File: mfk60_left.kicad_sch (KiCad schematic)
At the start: 27 parts, among them J1 USB_C_Receptacle_USB2.0, J2 ISP, J3 TRRS Jack, SW1 RST, T1 Tab, T2 Tab, T3 Tab, U1 ATmega32U4-M, Y1 16M

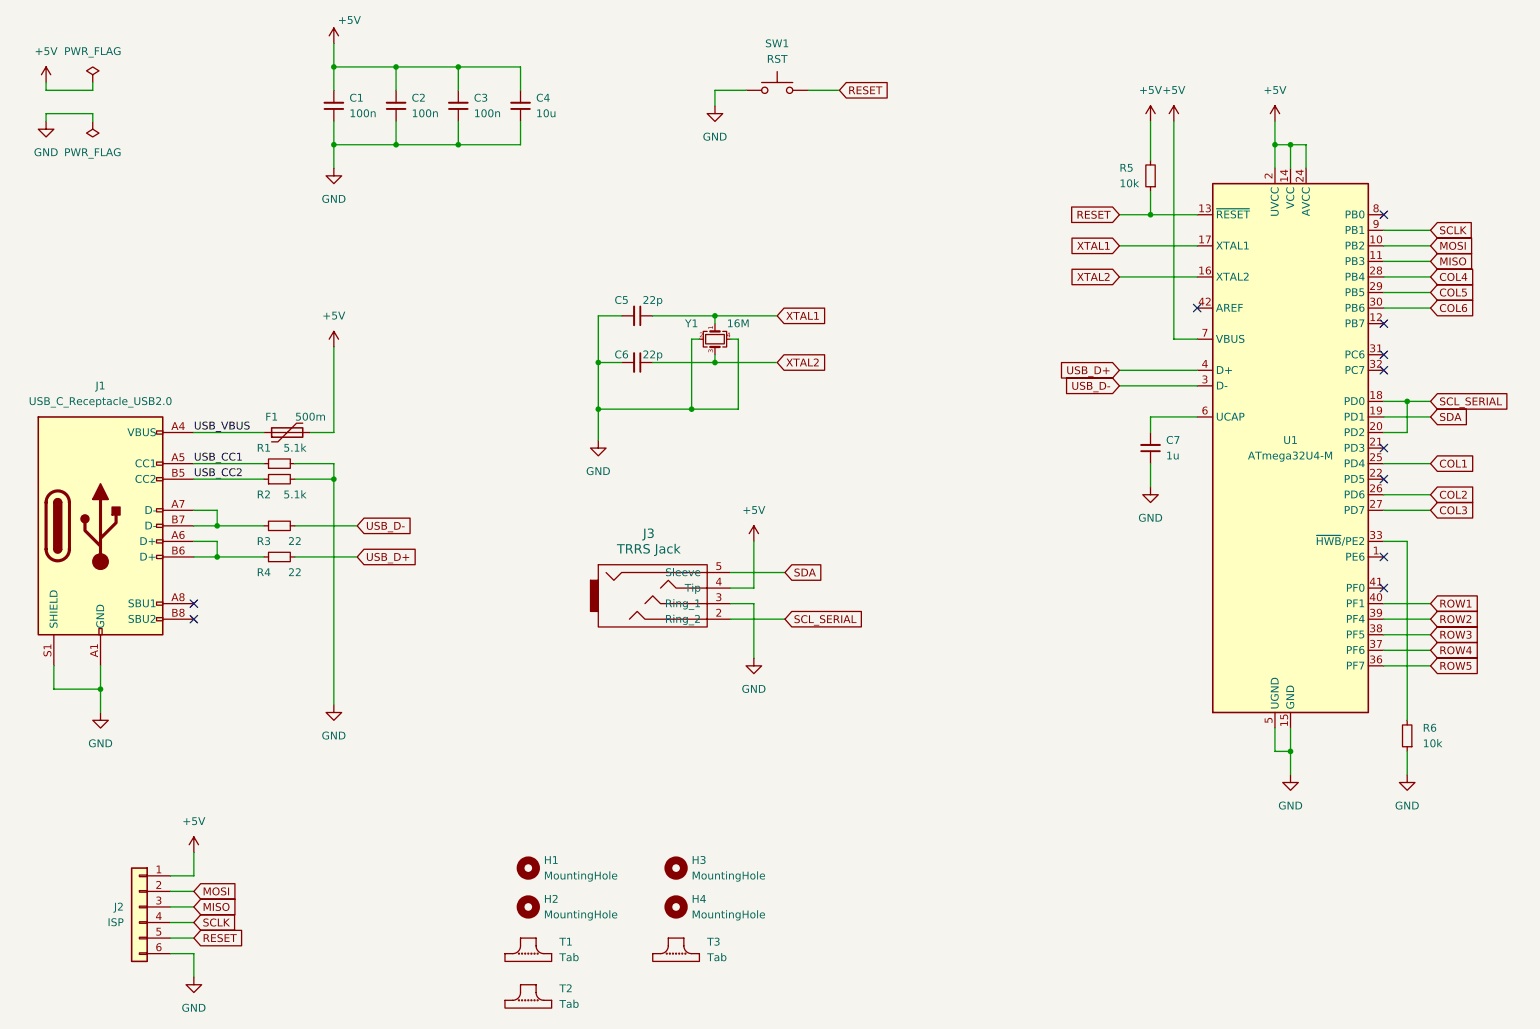
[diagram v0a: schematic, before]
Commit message: Add pull-up resistor on left side.
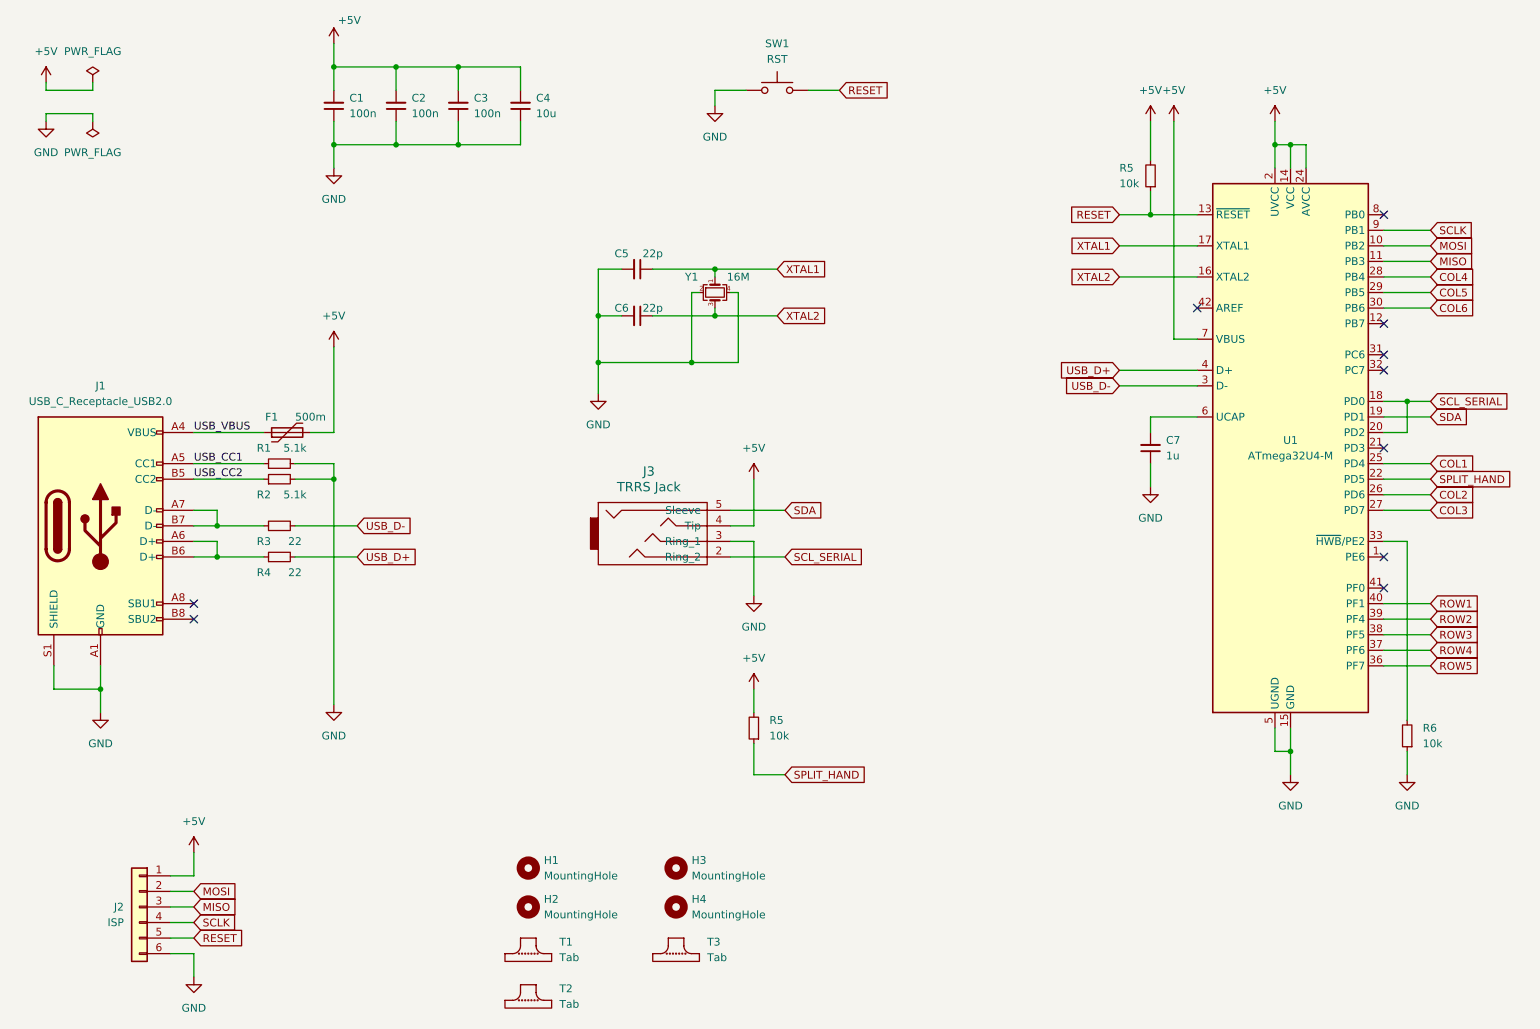
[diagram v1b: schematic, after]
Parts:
- added R5: 10k, Resistor_SMD:R_0805_2012Metric_Pad1.20x1.40mm_HandSolder, symbol Device:R_Small
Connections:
- net +5V: now also R5.2
- net SPLIT_HAND: now reaches U1.22 (PD5)
- net SPLIT_HAND: now also R5.1
- no-connect marks 11 -> 10
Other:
- moved on the sheet: C5, C6, J3, Y1

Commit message: FIX: key and diode value
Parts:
- J3: LCSC (none) -> C431535
- SW1: LCSC (none) -> C139797
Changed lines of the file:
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@@
+      (effects (font (size 1.27 1.27)) hide)
+    )
+    (property "Matrix" "" (at 226.06 91.44 0)
       (effects (font (size 1.27 1.27)) hide)
     )
@@
       (effects (font (size 1.27 1.27)) hide)
     )
+    (property "Matrix" "" (at 101.6 166.37 0)
+      (effects (font (size 1.27 1.27)) hide)
+    )
     (instances
       (project "mfk60"
@@
     )
     (property "LCSC" "C1804" (at 119.38 69.85 0)
+      (effects (font (size 1.27 1.27)) hide)
+    )
+    (property "Matrix" "" (at 119.38 69.85 0)
       (effects (font (size 1.27 1.27)) hide)
     )
@@
       (effects (font (size 1.27 1.27)) hide)
     )
+    (property "Matrix" "" (at 203.2 46.99 0)
+      (effects (font (size 1.27 1.27)) hide)
+    )
     (pin "1")
     (pin "2")
@@
     )
     (property "Datasheet" "~" (at 142.24 27.94 0)
+      (effects (font (size 1.27 1.27)) hide)
+    )
+    (property "Matrix" "" (at 142.24 33.02 0)
+      (effects (font (size 1.27 1.27)) hide)
+    )
+    (property "LCSC" "C139797" (at 142.24 33.02 0)
       (effects (font (size 1.27 1.27)) hide)
     )
@@
       (effects (font (size 1.27 1.27)) hide)
     )
+    (property "Matrix" "" (at 60.96 93.98 0)
+      (effects (font (size 1.27 1.27)) hide)
+    )
     (pin "1")
     (pin "2")
@@
       (effects (font (size 1.27 1.27)) hide)
     )
+    (property "Matrix" "" (at 119.38 62.23 0)
+      (effects (font (size 1.27 1.27)) hide)
+    )
     (pin "1")
     (pin "2")
@@
       (effects (font (size 1.27 1.27)) hide)
     )
+    (property "Matrix" "" (at 100.33 35.56 0)
+      (effects (font (size 1.27 1.27)) hide)
+    )
     (pin "1")
     (pin "2")
@@
     )
     (property "LCSC" "C28323" (at 203.2 91.44 0)
+      (effects (font (size 1.27 1.27)) hide)
+    )
+    (property "Matrix" "" (at 203.2 91.44 0)
       (effects (font (size 1.27 1.27)) hide)
     )
@@
       (effects (font (size 1.27 1.27)) hide)
     )
+    (property "Matrix" "" (at 101.6 173.99 0)
+      (effects (font (size 1.27 1.27)) hide)
+    )
     (instances
       (project "mfk60"
@@
       (effects (font (size 1.27 1.27)) hide)
     )
+    (property "Matrix" "" (at 60.96 96.52 0)
+      (effects (font (size 1.27 1.27)) hide)
+    )
     (pin "1")
     (pin "2")
@@
     )
     (property "Datasheet" "~" (at 101.6 160.02 0)
+      (effects (font (size 1.27 1.27)) hide)
+    )
+    (property "Matrix" "" (at 101.6 160.02 0)
       (effects (font (size 1.27 1.27)) hide)
     )
@@
       (effects (font (size 1.27 1.27)) hide)
     )
+    (property "Matrix" "" (at 101.6 181.61 0)
+      (effects (font (size 1.27 1.27)) hide)
+    )
     (instances
       (project "mfk60"
@@
       (effects (font (size 1.27 1.27)) hide)
     )
+    (property "Matrix" "" (at 60.96 109.22 0)
+      (effects (font (size 1.27 1.27)) hide)
+    )
     (pin "1")
     (pin "2")
@@
     )
     (property "LCSC" "C255949" (at 132.08 66.04 0)
+      (effects (font (size 1.27 1.27)) hide)
+    )
+    (property "Matrix" "" (at 132.08 66.04 0)
       (effects (font (size 1.27 1.27)) hide)
     )
@@
       (effects (font (size 1.27 1.27)) hide)
     )
+    (property "Matrix" "" (at 125.73 173.99 0)
+      (effects (font (size 1.27 1.27)) hide)
+    )
     (instances
       (project "mfk60"
@@
     )
     (property "LCSC" "C49678" (at 69.85 35.56 0)
+      (effects (font (size 1.27 1.27)) hide)
+    )
+    (property "Matrix" "" (at 69.85 35.56 0)
       (effects (font (size 1.27 1.27)) hide)
     )
@@
       (effects (font (size 1.27 1.27)) hide)
     )
+    (property "Matrix" "" (at 62.23 88.9 0)
+      (effects (font (size 1.27 1.27)) hide)
+    )
     (pin "1")
     (pin "2")
@@
       (effects (font (size 1.524 1.524)) hide)
     )
-    (property "LCSC" "" (at 121.92 105.41 0)
+    (property "LCSC" "C431535" (at 121.92 105.41 0)
+      (effects (font (size 1.27 1.27)) hide)
+    )
+    (property "Matrix" "" (at 121.92 105.41 0)
       (effects (font (size 1.27 1.27)) hide)
     )
@@
     )
     (property "LCSC" "C2982555" (at 31.75 104.14 0)
+      (effects (font (size 1.27 1.27)) hide)
+    )
+    (property "Matrix" "" (at 31.75 104.14 0)
       (effects (font (size 1.27 1.27)) hide)
     )
@@
       (effects (font (size 1.27 1.27)) hide)
     )
+    (property "Matrix" "" (at 80.01 35.56 0)
+      (effects (font (size 1.27 1.27)) hide)
+    )
     (pin "1")
     (pin "2")
@@
     )
     (property "LCSC" "" (at 38.1 166.37 0)
+      (effects (font (size 1.27 1.27)) hide)
+    )
+    (property "Matrix" "" (at 38.1 166.37 0)
       (effects (font (size 1.27 1.27)) hide)
     )
@@
       (effects (font (size 1.27 1.27)) hide)
     )
+    (property "Matrix" "" (at 245.11 138.43 0)
+      (effects (font (size 1.27 1.27)) hide)
+    )
     (pin "1")
     (pin "2")
@@
     )
     (property "Datasheet" "~" (at 125.73 166.37 0)
+      (effects (font (size 1.27 1.27)) hide)
+    )
+    (property "Matrix" "" (at 125.73 166.37 0)
       (effects (font (size 1.27 1.27)) hide)
     )
@@
       (effects (font (size 1.27 1.27)) hide)
     )
+    (property "Matrix" "" (at 60.96 104.14 0)
+      (effects (font (size 1.27 1.27)) hide)
+    )
     (pin "1")
     (pin "2")
@@
       (effects (font (size 1.27 1.27)) hide)
     )
+    (property "Matrix" "" (at 90.17 35.56 0)
+      (effects (font (size 1.27 1.27)) hide)
+    )
     (pin "1")
     (pin "2")
@@
       (effects (font (size 1.27 1.27)) hide)
     )
+    (property "Matrix" "" (at 138.43 137.16 0)
+      (effects (font (size 1.27 1.27)) hide)
+    )
     (pin "1")
     (pin "2")
@@
       (effects (font (size 1.27 1.27)) hide)
     )
+    (property "Matrix" "" (at 125.73 160.02 0)
+      (effects (font (size 1.27 1.27)) hide)
+    )
